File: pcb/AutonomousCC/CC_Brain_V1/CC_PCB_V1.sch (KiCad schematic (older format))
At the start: 15 parts, among them J1 Screw_Terminal_01x07, J2 Antenna_Conn_02x04_Odd_Even, J3 USB1130-15-A_REVA, J5 Relay_Conn_01x06, U1 Pico, U2 LM337_TO3

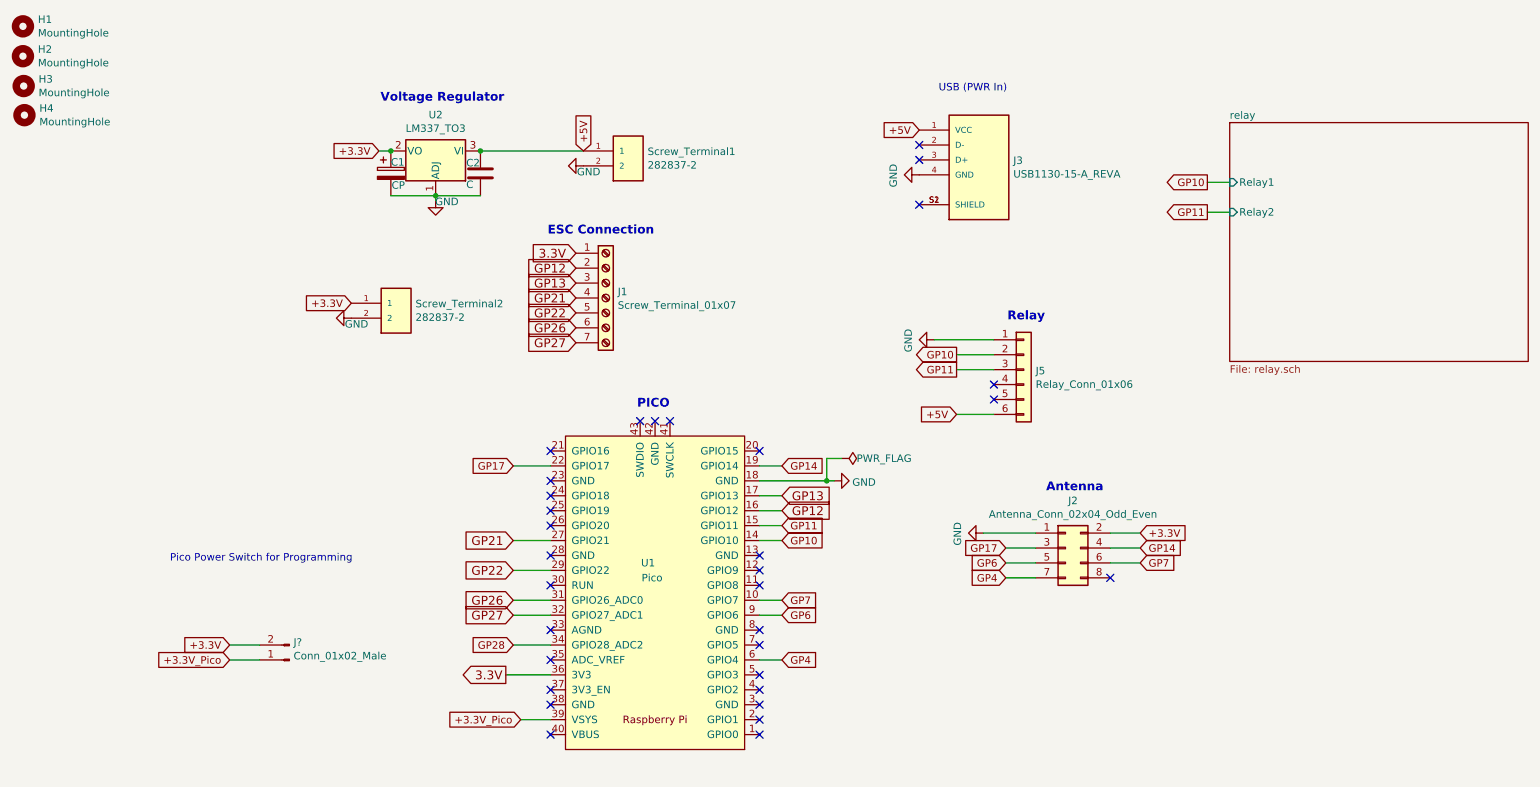
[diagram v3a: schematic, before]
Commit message: Added most of the footprints
Still need Diodes, Resistors (if THT or SMD), and LED footprints
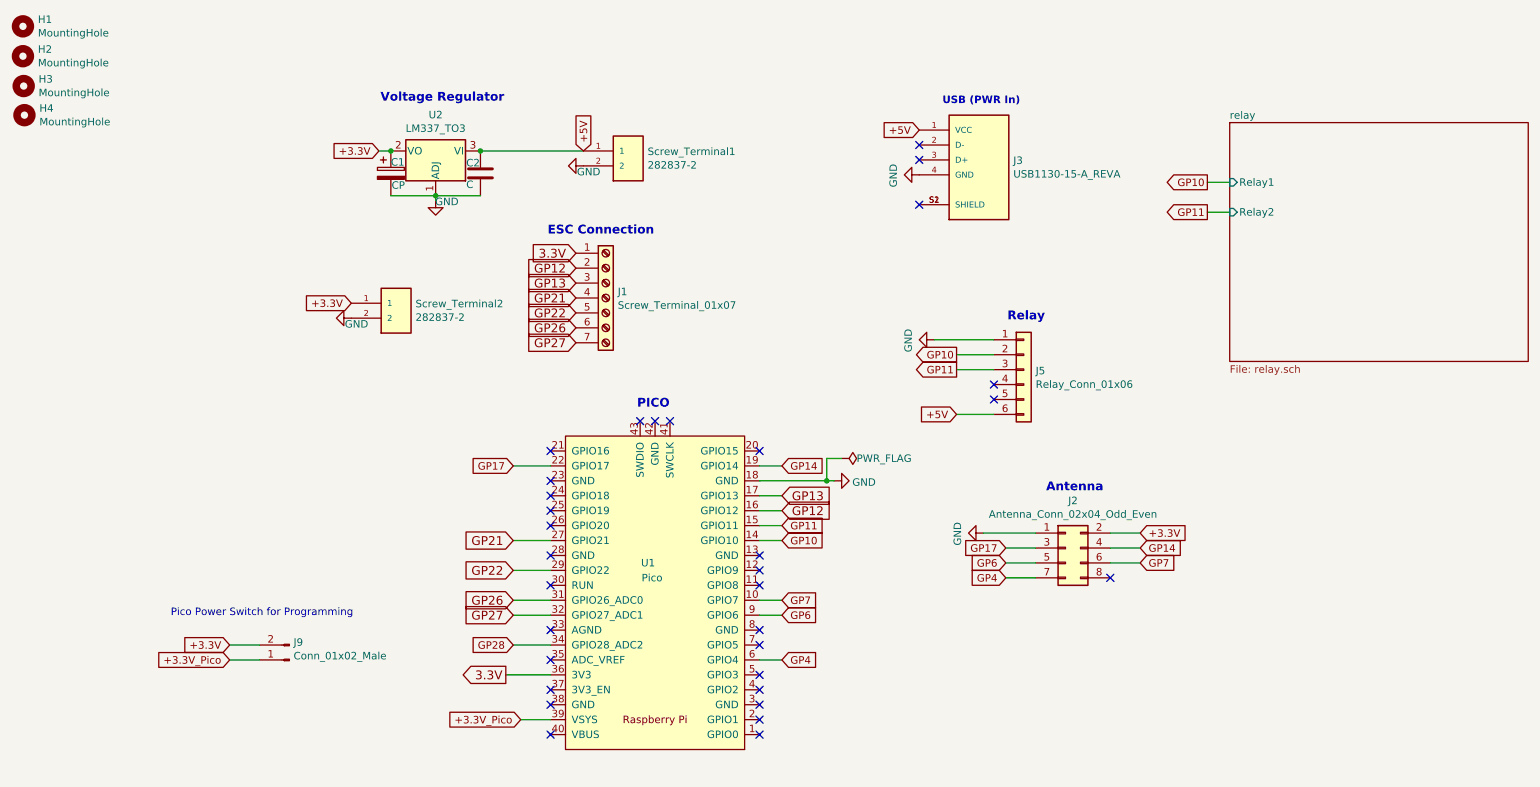
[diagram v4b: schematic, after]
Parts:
- J9: renamed from J?; footprint (none) -> Connector_PinHeader_2.54mm:PinHeader_1x02_P2.54mm_Vertical
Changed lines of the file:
@@
 encoding utf-8
 Sheet 1 2
-Title "Autonomous Crazy Cart V1"
+Title "Autonomous Crazy Cart V2"
 Date "09/12/2021"
 Rev "09/18/2021"
 Comp "Engineering Physics Propulsion Lab * EPPL *"
-Comment1 "might need future revisions"
-Comment2 ""
-Comment3 ""
-Comment4 ""
+Comment1 ""
+Comment2 "Made Relay and Radio module pins bigger (2.45mm)"
+Comment3 "Relay Circuit"
+Comment4 "Added: Switch for PICO V"
 $EndDescr
 $Comp
@@
 Text GLabel 2150 4850 0    50   Input ~ 0
 +3.3V
-Text Notes 1750 4300 0    50   ~ 0
+Text Notes 1755 4665 0    50   ~ 0
 Pico Power Switch for Programming\n
-Text Notes 6900 1150 0    50   ~ 0
+Text Notes 6925 1235 0    50   ~ 10
 USB (PWR In)\n
 Wire Wire Line
@@
 GP11
 $Comp
-L Connector:Conn_01x02_Male J?
+L Connector:Conn_01x02_Male J9
 U 1 1 61610430
 P 2550 4950
-F 0 "J?" H 2522 4832 50  0000 R CNN
+F 0 "J9" H 2522 4832 50  0000 R CNN
 F 1 "Conn_01x02_Male" H 2522 4923 50  0000 R CNN
-F 2 "" H 2550 4950 50  0001 C CNN
+F 2 "Connector_PinHeader_2.54mm:PinHeader_1x02_P2.54mm_Vertical" H 2550 4950 50  0001 C CNN
 F 3 "~" H 2550 4950 50  0001 C CNN
 	1    2550 4950

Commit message: Updated Footprint and Fixed PCB Layout
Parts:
- C1, C2: footprint Capacitor_THT:CP_Radial_D8.0mm_P5.00mm -> Capacitor_THT:CP_Radial_D4.0mm_P1.50mm
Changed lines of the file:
@@
 F 0 "C2" H 3735 1760 50  0000 L CNN
 F 1 "C" H 3735 1615 50  0000 L CNN
-F 2 "Capacitor_THT:CP_Radial_D8.0mm_P5.00mm" H 3868 1540 50  0001 C CNN
+F 2 "Capacitor_THT:CP_Radial_D4.0mm_P1.50mm" H 3868 1540 50  0001 C CNN
 F 3 "https://www.vishay.com/docs/28549/dseries.pdf" H 3830 1690 50  0001 C CNN
 	1    3830 1690
@@
 F 0 "C1" H 3230 1765 50  0000 L CNN
 F 1 "CP" H 3235 1610 50  0000 L CNN
-F 2 "Capacitor_THT:CP_Radial_D8.0mm_P5.00mm" H 3268 1540 50  0001 C CNN
+F 2 "Capacitor_THT:CP_Radial_D4.0mm_P1.50mm" H 3268 1540 50  0001 C CNN
 F 3 "https://www.tdk-electronics.tdk.com/inf/20/30/db/aec/B41866.pdf" H 3230 1690 50  0001 C CNN
 	1    3230 1690

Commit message: OK, OK now we are done
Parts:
- added D5, D6: SMD LED2, LED_SMD:LED_1206_3216Metric_Pad1.42x1.75mm_HandSolder, symbol Device:LED
- added R5, R6: 1k, Resistor_SMD:R_0603_1608Metric_Pad0.98x0.95mm_HandSolder, symbol Device:R_Small_US
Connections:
- net GP12: now also R6.2
- net GP22: now also R5.2
- new net: D6.2 (A), R6.1
- new net: D5.2 (A), R5.1
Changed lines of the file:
@@
 Title "Autonomous Crazy Cart V2"
 Date "09/12/2021"
-Rev "09/18/2021"
+Rev "10/13/2021"
 Comp "Engineering Physics Propulsion Lab * EPPL *"
 Comment1 ""
@@
 P 6250 3600
 F 0 "#FLG0103" H 6250 3675 50  0001 C CNN
-F 1 "PWR_FLAG" V 6250 3700 50  0000 L CNN
+F 1 "PWR_FLAG" V 6165 3390 50  0000 L CNN
 F 2 "" H 6250 3600 50  0001 C CNN
 F 3 "~" H 6250 3600 50  0001 C CNN
@@
 Text GLabel 4470 2825 0    59   Input ~ 0
 GP27
-Text GLabel 5850 3950 2    59   Input ~ 0
+Text GLabel 6900 3950 2    59   Input ~ 0
 GP12
 Text GLabel 5850 3850 2    59   Input ~ 0
@@
 Text GLabel 4050 4150 0    59   Input ~ 0
 GP21
-Text GLabel 4050 4350 0    59   Input ~ 0
+Text GLabel 3540 4350 0    59   Input ~ 0
 GP22
 Text GLabel 4050 4550 0    59   Input ~ 0
@@
 	5700 3850 5850 3850
 Wire Wire Line
-	5850 3950 5700 3950
-Wire Wire Line
 	5700 4050 5850 4050
 Wire Wire Line
@@
 Wire Wire Line
 	4300 4550 4050 4550
-Wire Wire Line
-	4050 4350 4300 4350
 Wire Wire Line
 	4300 4150 4050 4150
@@
 Wire Wire Line
 	2150 4950 2350 4950
+$Comp
+L Device:R_Small_US R?
+U 1 1 616756D3
+P 6575 3850
+AR Path="/615DA4AF/616756D3" Ref="R?"  Part="1"
+AR Path="/616756D3" Ref="R6"  Part="1"
+F 0 "R6" H 6620 3900 50  0000 L CNN
+F 1 "1k" H 6605 3795 50  0000 L CNN
+F 2 "Resistor_SMD:R_0603_1608Metric_Pad0.98x0.95mm_HandSolder" H 6575 3850 50  0001 C CNN
+F 3 "~" H 6575 3850 50  0001 C CNN
+	1    6575 3850
+	1    0    0    -1
+$EndComp
+$Comp
+L Device:R_Small_US R?
+U 1 1 61676AAC
+P 3685 4250
+AR Path="/615DA4AF/61676AAC" Ref="R?"  Part="1"
+AR Path="/61676AAC" Ref="R5"  Part="1"
+F 0 "R5" H 3570 4300 50  0000 L CNN
+F 1 "1k" H 3715 4190 50  0000 L CNN
+F 2 "Resistor_SMD:R_0603_1608Metric_Pad0.98x0.95mm_HandSolder" H 3685 4250 50  0001 C CNN
+F 3 "~" H 3685 4250 50  0001 C CNN
+	1    3685 4250
+	1    0    0    -1
+$EndComp
+$Comp
+L Device:LED D?
+U 1 1 616797FD
+P 6575 3525
+AR Path="/615DA4AF/616797FD" Ref="D?"  Part="1"
+AR Path="/616797FD" Ref="D6"  Part="1"
+F 0 "D6" V 6665 3575 50  0000 C CNN
+F 1 "SMD LED2" V 6360 3520 50  0000 C CNN
+F 2 "LED_SMD:LED_1206_3216Metric_Pad1.42x1.75mm_HandSolder" H 6575 3525 50  0001 C CNN
+F 3 "~" H 6575 3525 50  0001 C CNN
+	1    6575 3525
+	0    1    1    0
+$EndComp
+$Comp
+L Device:LED D?
+U 1 1 6167A748
+P 3685 3925
+AR Path="/615DA4AF/6167A748" Ref="D?"  Part="1"
+AR Path="/6167A748" Ref="D5"  Part="1"
+F 0 "D5" V 3785 3980 50  0000 C CNN
+F 1 "SMD LED2" V 3465 3860 50  0000 C CNN
+F 2 "LED_SMD:LED_1206_3216Metric_Pad1.42x1.75mm_HandSolder" H 3685 3925 50  0001 C CNN
+F 3 "~" H 3685 3925 50  0001 C CNN
+	1    3685 3925
+	0    1    1    0
+$EndComp
+Wire Wire Line
+	5700 3950 6575 3950
+Connection ~ 6575 3950
+Wire Wire Line
+	6575 3950 6900 3950
+Wire Wire Line
+	6575 3675 6575 3750
+Wire Wire Line
+	3540 4350 3685 4350
+Connection ~ 3685 4350
+Wire Wire Line
+	3685 4350 4300 4350
+Wire Wire Line
+	3685 4075 3685 4150
 $EndSCHEMATC

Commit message: CC Controller and Brain VERSION 1.1
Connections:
- net GND: now also D5.1 (K), D6.1 (K)
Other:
- moved on the sheet: D5, D6, R5, R6
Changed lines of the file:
@@
 L Device:R_Small_US R?
 U 1 1 616756D3
-P 6575 3850
+P 6650 3850
 AR Path="/615DA4AF/616756D3" Ref="R?"  Part="1"
 AR Path="/616756D3" Ref="R6"  Part="1"
-F 0 "R6" H 6620 3900 50  0000 L CNN
-F 1 "1k" H 6605 3795 50  0000 L CNN
-F 2 "Resistor_SMD:R_0603_1608Metric_Pad0.98x0.95mm_HandSolder" H 6575 3850 50  0001 C CNN
-F 3 "~" H 6575 3850 50  0001 C CNN
-	1    6575 3850
+F 0 "R6" H 6695 3900 50  0000 L CNN
+F 1 "1k" H 6680 3795 50  0000 L CNN
+F 2 "Resistor_SMD:R_0603_1608Metric_Pad0.98x0.95mm_HandSolder" H 6650 3850 50  0001 C CNN
+F 3 "~" H 6650 3850 50  0001 C CNN
+	1    6650 3850
 	1    0    0    -1
 $EndComp
@@
 L Device:R_Small_US R?
 U 1 1 61676AAC
-P 3685 4250
+P 3650 4250
 AR Path="/615DA4AF/61676AAC" Ref="R?"  Part="1"
 AR Path="/61676AAC" Ref="R5"  Part="1"
-F 0 "R5" H 3570 4300 50  0000 L CNN
-F 1 "1k" H 3715 4190 50  0000 L CNN
-F 2 "Resistor_SMD:R_0603_1608Metric_Pad0.98x0.95mm_HandSolder" H 3685 4250 50  0001 C CNN
-F 3 "~" H 3685 4250 50  0001 C CNN
-	1    3685 4250
+F 0 "R5" H 3535 4300 50  0000 L CNN
+F 1 "1k" H 3680 4190 50  0000 L CNN
+F 2 "Resistor_SMD:R_0603_1608Metric_Pad0.98x0.95mm_HandSolder" H 3650 4250 50  0001 C CNN
+F 3 "~" H 3650 4250 50  0001 C CNN
+	1    3650 4250
 	1    0    0    -1
 $EndComp
@@
 L Device:LED D?
 U 1 1 616797FD
-P 6575 3525
+P 6650 3500
 AR Path="/615DA4AF/616797FD" Ref="D?"  Part="1"
 AR Path="/616797FD" Ref="D6"  Part="1"
-F 0 "D6" V 6665 3575 50  0000 C CNN
-F 1 "SMD LED2" V 6360 3520 50  0000 C CNN
-F 2 "LED_SMD:LED_1206_3216Metric_Pad1.42x1.75mm_HandSolder" H 6575 3525 50  0001 C CNN
-F 3 "~" H 6575 3525 50  0001 C CNN
-	1    6575 3525
+F 0 "D6" V 6740 3550 50  0000 C CNN
+F 1 "SMD LED2" V 6625 3775 50  0000 C CNN
+F 2 "LED_SMD:LED_1206_3216Metric_Pad1.42x1.75mm_HandSolder" H 6650 3500 50  0001 C CNN
+F 3 "~" H 6650 3500 50  0001 C CNN
+	1    6650 3500
 	0    1    1    0
 $EndComp
@@
 L Device:LED D?
 U 1 1 6167A748
-P 3685 3925
+P 3650 3900
 AR Path="/615DA4AF/6167A748" Ref="D?"  Part="1"
 AR Path="/6167A748" Ref="D5"  Part="1"
-F 0 "D5" V 3785 3980 50  0000 C CNN
-F 1 "SMD LED2" V 3465 3860 50  0000 C CNN
-F 2 "LED_SMD:LED_1206_3216Metric_Pad1.42x1.75mm_HandSolder" H 3685 3925 50  0001 C CNN
-F 3 "~" H 3685 3925 50  0001 C CNN
-	1    3685 3925
+F 0 "D5" V 3750 3955 50  0000 C CNN
+F 1 "SMD LED2" V 3625 3615 50  0000 C CNN
+F 2 "LED_SMD:LED_1206_3216Metric_Pad1.42x1.75mm_HandSolder" H 3650 3900 50  0001 C CNN
+F 3 "~" H 3650 3900 50  0001 C CNN
+	1    3650 3900
 	0    1    1    0
 $EndComp
 Wire Wire Line
-	5700 3950 6575 3950
-Connection ~ 6575 3950
+	3540 4350 3650 4350
+Connection ~ 3650 4350
 Wire Wire Line
-	6575 3950 6900 3950
+	3650 4350 4300 4350
 Wire Wire Line
-	6575 3675 6575 3750
+	3650 4050 3650 4150
+$Comp
+L CC_PCB_V1-rescue:GND-power #PWR?
+U 1 1 616D58BC
+P 3650 3600
+F 0 "#PWR?" H 3650 3350 50  0001 C CNN
+F 1 "GND" V 3690 3635 50  0000 C CNN
+F 2 "" H 3650 3600 50  0001 C CNN
+F 3 "" H 3650 3600 50  0001 C CNN
+	1    3650 3600
+	-1   0    0    1
+$EndComp
 Wire Wire Line
-	3540 4350 3685 4350
-Connection ~ 3685 4350
+	3650 3600 3650 3750
+$Comp
+L CC_PCB_V1-rescue:GND-power #PWR?
+U 1 1 616DC890
+P 6650 3200
+F 0 "#PWR?" H 6650 2950 50  0001 C CNN
+F 1 "GND" V 6690 3235 50  0000 C CNN
+F 2 "" H 6650 3200 50  0001 C CNN
+F 3 "" H 6650 3200 50  0001 C CNN
+	1    6650 3200
+	-1   0    0    1
+$EndComp
+Connection ~ 6650 3950
 Wire Wire Line
-	3685 4350 4300 4350
+	6650 3950 6900 3950
 Wire Wire Line
-	3685 4075 3685 4150
+	5700 3950 6650 3950
+Wire Wire Line
+	6650 3750 6650 3650
+Wire Wire Line
+	6650 3200 6650 3350
 $EndSCHEMATC
